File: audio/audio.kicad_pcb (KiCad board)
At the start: 2 copper layers, 67 parts, among them P1 CONN_02X01, P2 CONN_01X04, P3 CONN_02X01, P4 CONN_02X01, U1 PCM2912A, U2 USBAM, U3 MIC, U4 FB, U5 FB, U6 NAU8223, U7 FB, U8 FB, X1 6MHz

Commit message: audio pcb updates
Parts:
- removed U8: FB, SMD_Packages:SMD-1210
- added 1PIN: P***, Connect:1pin, F.Cu at (127.8, 114.1)
- added 2PIN: P***, Connect:1pin, F.Cu at (127.8, 94.1)
- added 3PIN: P***, Connect:1pin, F.Cu at (173.8, 94.1)
- added 4PIN: P***, Connect:1pin, F.Cu at (173.8, 114.1)
- added USB1: AB2_USB, AB2USB:AB2_USB_MICRO_SMD, F.Cu at (124.8, 104.1)
- C1, C10, C11, C12, C13, C14, C15, C16, C17, C3, C4, C5, C8, C9: footprint SMD_Packages:SMD-0603_c -> SMD_Packages:SMD-0603; moved to B.Cu
- C18: value C -> 0.1uF; footprint SMD_Packages:SMD-0603_c -> SMD_Packages:SMD-0603
- C19, C24, C27, C33: value C -> 10uF; footprint SMD_Packages:SMD-0603_c -> SMD_Packages:SMD-0603; moved to B.Cu
- C20, C22, C29, C31: value C -> 1nF; footprint SMD_Packages:SMD-0603_c -> SMD_Packages:SMD-0603; moved to B.Cu
- C21, C23, C28, C30: value C -> 0.47uF; footprint SMD_Packages:SMD-0603_c -> SMD_Packages:SMD-0603; moved to B.Cu
- C25, C26, C32: value C -> 0.1uF; footprint SMD_Packages:SMD-0603_c -> SMD_Packages:SMD-0603; moved to B.Cu
- C6: footprint SMD_Packages:SMD-0603_c -> SMD_Packages:SMD-0603
- JP1: value JUMPER -> HGAIN
- JP2: value JUMPER -> LGAIN
- JP3: value JUMPER -> XMIC
- JP4: value JUMPER -> GS5
- JP5: value JUMPER -> GS0
- L1: moved to B.Cu
- R1, R10, R11, R2, R3, R4, R6, R8: footprint SMD_Packages:SMD-0603_r -> SMD_Packages:SMD-0603; moved to B.Cu
- R5, R7, R9: footprint SMD_Packages:SMD-0603_r -> SMD_Packages:SMD-0603
- SP1: value SPEAKER -> RIGHT
- SP2: value SPEAKER -> LEFT
- U2: value USBAM -> MIC; footprint Connect:USB_A -> MIC:MIC
- U3: value MIC -> FB; footprint MIC:MIC -> MIC:FB-28F0121
- U4, U7: footprint SMD_Packages:SMD-1210 -> MIC:FB-28F0121
- U5: value FB -> NAU8223; footprint SMD_Packages:SMD-1210 -> MIC:QFN20
- U6: value NAU8223 -> FB; footprint MIC:QFN20 -> MIC:FB-28F0121
- X1: footprint SMD_Packages:SMD-1210 -> MIC:FOX6MHZ; moved to B.Cu
- moved D2 70.2 mm to (131.8, 98.6)
- moved C18 68.0 mm to (133.1, 106.9), turned to 180 degrees
- moved C15 62.6 mm to (145.6, 97.1)
- moved JP5 60.3 mm to (156.8, 93.4), turned to 270 degrees
- moved X1 55.5 mm to (137.1, 94.4), turned to 180 degrees
- moved C17 54.9 mm to (149.6, 110.1)
- moved C20 51.7 mm to (162.3, 110.1)
- moved C12 51.6 mm to (145.6, 94.1)
- moved C16 51.6 mm to (158.1, 112.9), turned to 180 degrees
- moved JP1 49.3 mm to (147.1, 93.4), turned to 270 degrees
- moved C10 49.0 mm to (157.8, 94.1)
- moved C14 48.8 mm to (149.6, 99.6)
- moved U2 48.7 mm to (165.3, 93.6), turned to 270 degrees
- moved JP2 48.3 mm to (150.3, 93.4), turned to 270 degrees
- moved JP4 47.3 mm to (153.6, 93.4), turned to 270 degrees
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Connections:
- U2 pad 1: Net-(D1-Pad1) -> XOUT
- U2 pad 2: Net-(R5-Pad2) -> XGAIN
- U2 pad 3: Net-(R6-Pad2) -> Net-(C10-Pad2)
- U2 pad 5: XGND -> Net-(U2-Pad5)
- U2 pad 6: XGND -> Net-(JP3-Pad1)
- U3 pad 1: XOUT -> Net-(C20-Pad1)
- U3 pad 2: XGAIN -> Net-(U3-Pad2)
- U4 pad 1: Net-(C20-Pad1) -> Net-(C22-Pad1)
- U5 pad 1: Net-(C22-Pad1) -> Net-(U3-Pad2)
- U5 pad 2: Net-(U5-Pad2) -> +5VA
- U6 pad 1: Net-(U4-Pad2) -> Net-(C29-Pad1)
- U6 pad 2: +5VA -> Net-(U5-Pad17)
- U7 pad 1: Net-(C29-Pad1) -> Net-(C31-Pad1)
- U7 pad 2: Net-(U6-Pad17) -> Net-(U5-Pad15)
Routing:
- net +5VA: track 0.00 -> 146.8 mm, vias 0 -> 4
- net XGAIN: track 0.00 -> 77.4 mm, vias 0 -> 1
- net Net-(C9-Pad1): track 0.00 -> 69.6 mm, vias 0 -> 1
- net XOUT: track 0.00 -> 67.5 mm, vias 0 -> 1
- net Net-(C16-Pad1): track 0.00 -> 57.4 mm, vias 0 -> 1
- net Net-(R6-Pad2): track 0.00 -> 45.0 mm, vias 0 -> 2
- net EN: track 0.00 -> 43.3 mm, vias 0 -> 1
- net Net-(C2-Pad2): track 0.00 -> 38.7 mm, vias 0 -> 1
- net Net-(P1-Pad1): track 0.00 -> 37.8 mm
- net R_IN: track 0.00 -> 36.8 mm, vias 0 -> 2
- net Net-(C6-Pad2): track 0.00 -> 30.9 mm, vias 0 -> 1
- net Net-(D1-Pad1): track 0.00 -> 30.6 mm, vias 0 -> 1
- net Net-(C20-Pad1): track 0.00 -> 30.4 mm, vias 0 -> 1
- net Net-(C31-Pad1): track 0.00 -> 28.4 mm
- net L_IN: track 0.00 -> 27.1 mm, vias 0 -> 1
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- added copper zone on B.Cu, net XGND
- added copper zone on F.Cu, net XGND
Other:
- board outline added: 52 x 26 mm
- net class normal added: clearance 0.1524, trace_width 0.18, via_dia 0.604, via_drill 0.35
- net class power added: clearance 0.1524, trace_width 0.3, via_dia 0.889, via_drill 0.635
- rule trace_min: 0.254 -> 0.1524
- rule via_min_drill: 0.508 -> 0.35
- rule via_min_size: 0.889 -> 0.604

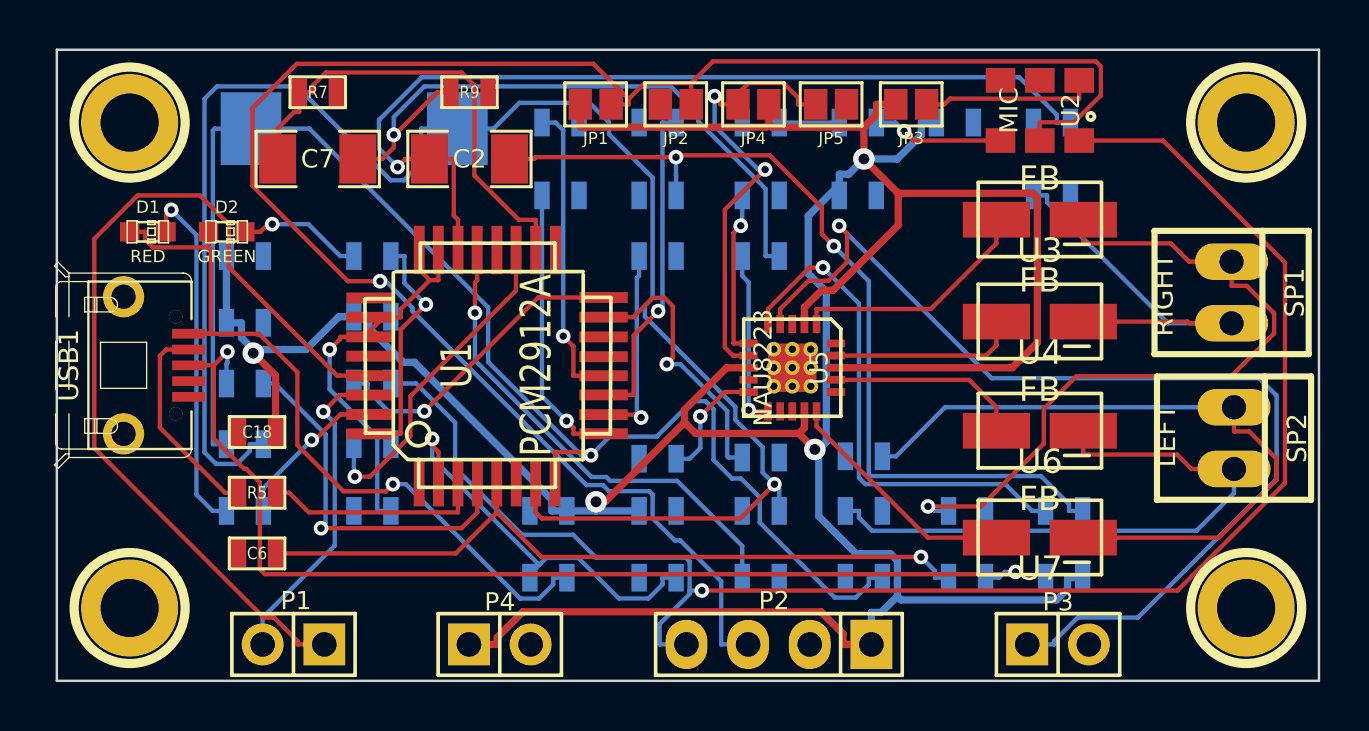
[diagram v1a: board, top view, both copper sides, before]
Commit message: finishing audio pcb layout
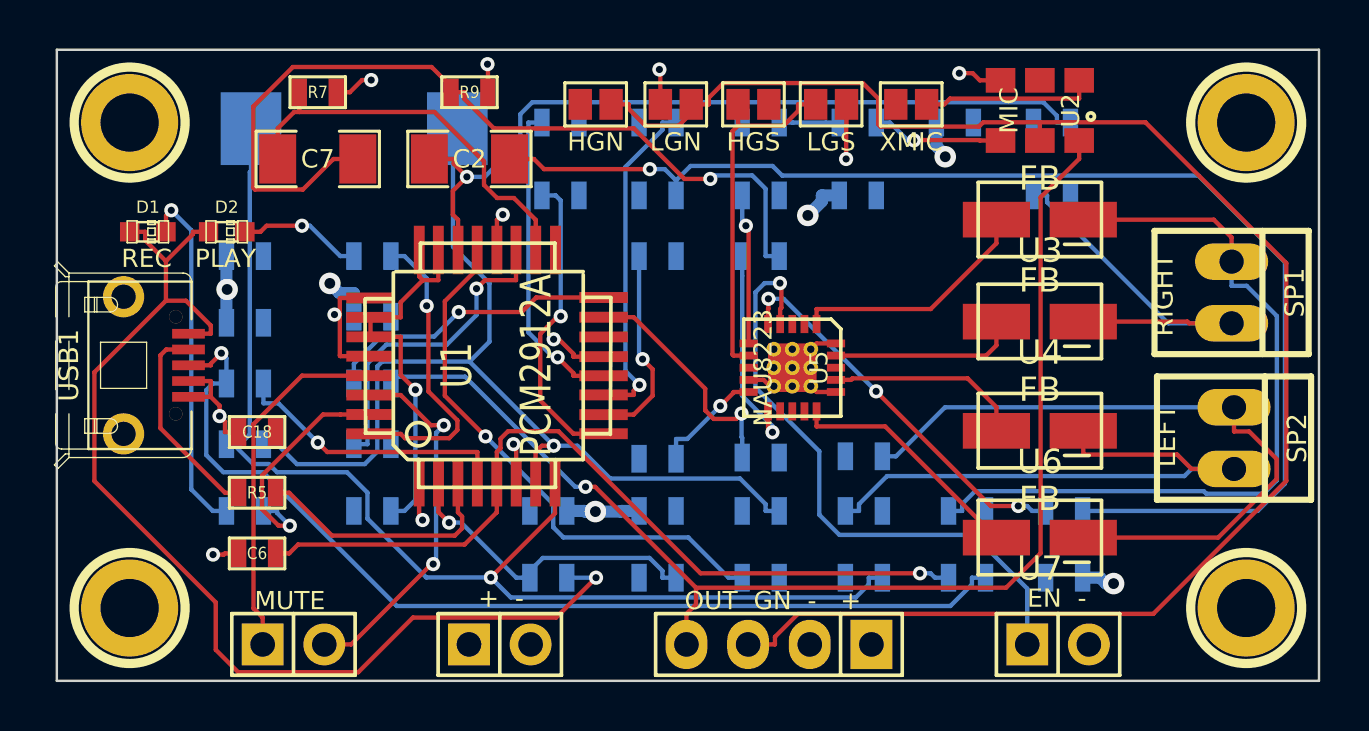
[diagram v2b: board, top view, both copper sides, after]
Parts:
- turned P1 to 270 degrees
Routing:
- net +5VA: track 146.8 -> 12.6 mm, vias 4 -> 6
- net XGND: track 0.00 -> 29.9 mm, vias 0 -> 12
- net Net-(C9-Pad1): track 69.6 -> 40.8 mm
- net Net-(P1-Pad1): track 37.8 -> 14.9 mm
- net EN: track 43.3 -> 25.3 mm
- net XOUT: track 67.5 -> 51.2 mm
- net R_IN: track 36.8 -> 52.7 mm, vias 2 -> 1
- net Net-(D1-Pad1): track 30.6 -> 46.2 mm
- net XGAIN: track 77.4 -> 68.2 mm, vias 1 -> 0
- net L_IN: track 27.1 -> 35.9 mm
- net Net-(C16-Pad1): track 57.4 -> 49.3 mm
- net Net-(C2-Pad2): track 38.7 -> 32.6 mm
- net Net-(C21-Pad1): track 21.1 -> 16.1 mm, vias 1 -> 3
- net Net-(JP4-Pad2): track 18.7 -> 14.8 mm, vias 2 -> 0
- net Net-(R6-Pad1): track 15.4 -> 11.7 mm
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- added copper zone on F.Cu, net +5VA
- removed copper zone on F.Cu, net XGND
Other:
- net class Default: clearance 0.254 -> 0.1524
- net class normal: via_dia 0.604 -> 0.5842; via_drill 0.35 -> 0.3302
- net class power: trace_width 0.3 -> 0.5
- rule trace_clearance: 0.254 -> 0.1524
- rule via_min_drill: 0.35 -> 0.3302
- rule via_min_size: 0.604 -> 0.5842
- board text added: "+ -"
- board text added: "EN -"
- board text added: "HGN"
- board text added: "HGS"
- board text added: "LGN"
- board text added: "LGS"
- board text added: "MUTE"
- board text added: "OUT GN - +"
- board text added: "PLAY"
- board text added: "REC"
- board text added: "XMIC"

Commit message: added logo mod, updated audio pcb, and finished micboard
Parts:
- added G***: LOGO, MIC:LOGO, B.Cu at (150.8, 104.1)

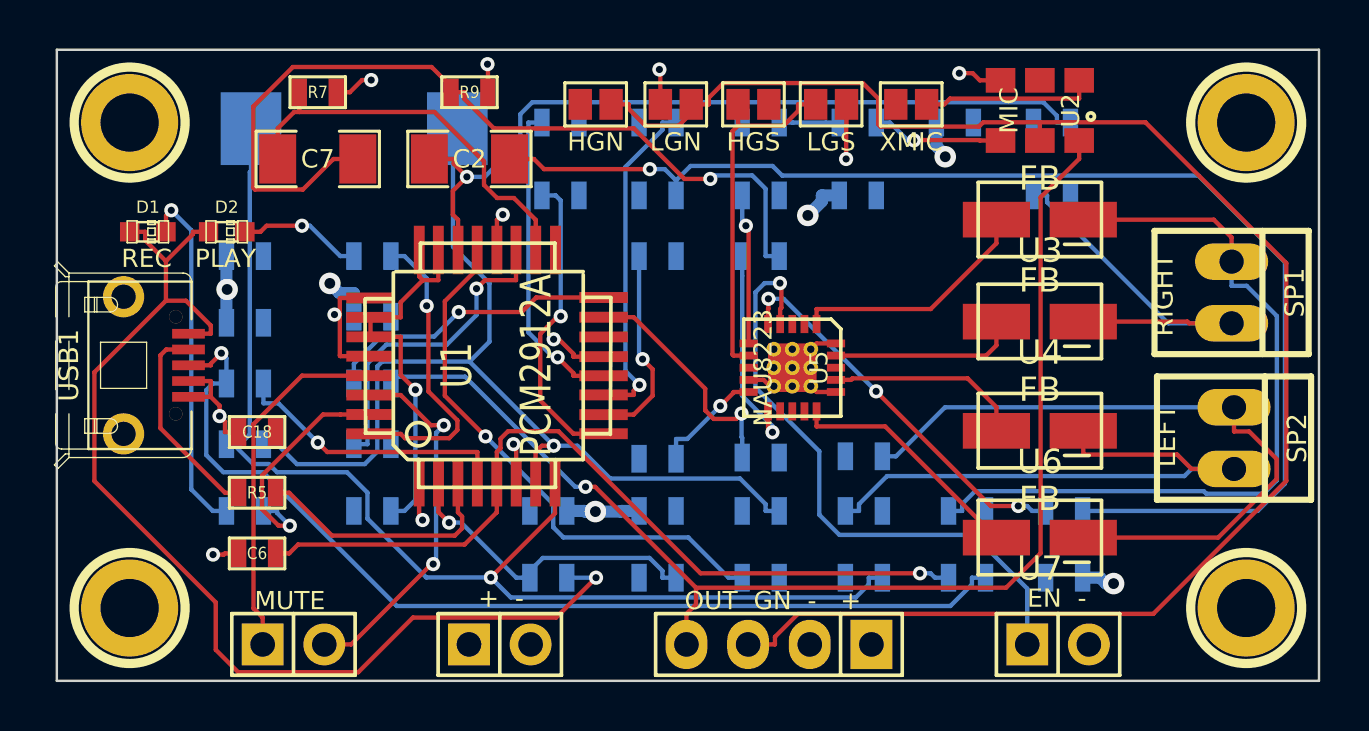
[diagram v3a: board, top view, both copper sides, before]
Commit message: updating audio board to change vias
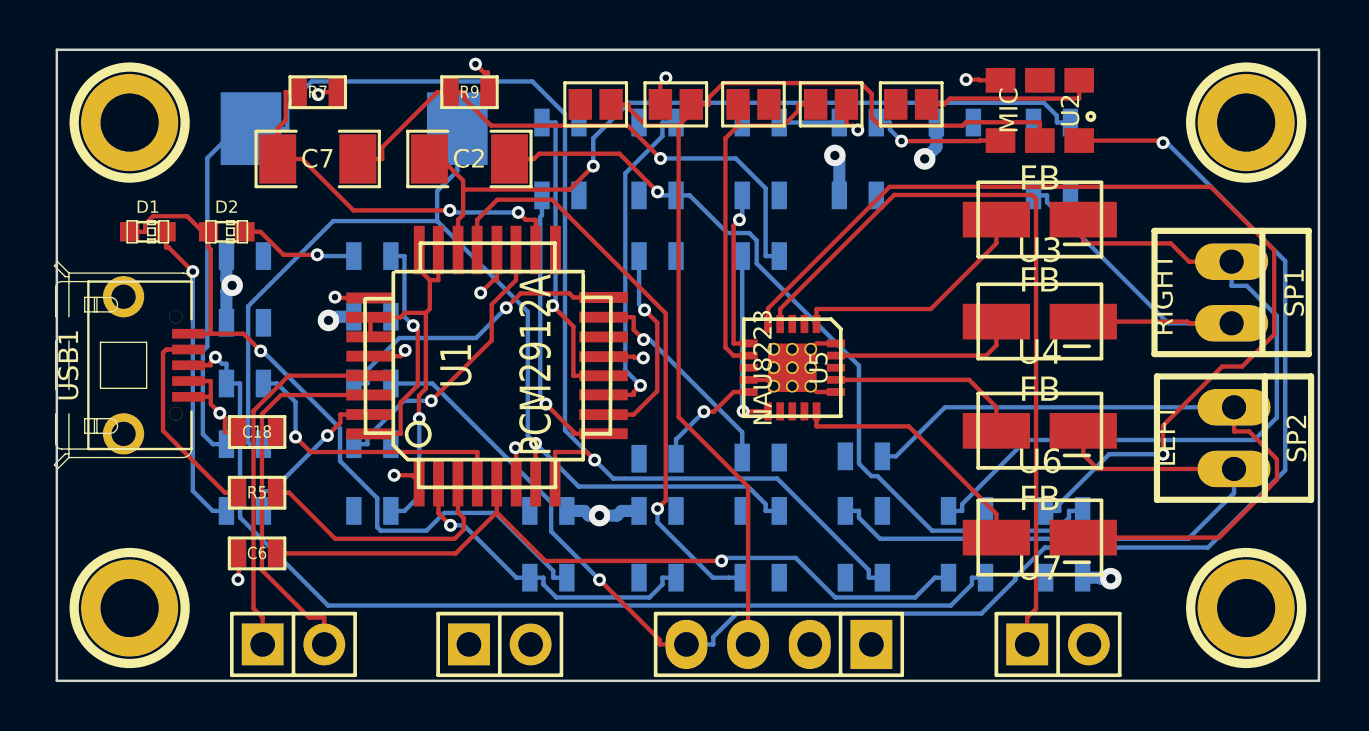
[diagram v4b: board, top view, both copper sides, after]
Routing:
- net Net-(C21-Pad1): track 16.1 -> 41.4 mm, vias 3 -> 1
- net XGAIN: track 68.2 -> 44.0 mm
- net R_IN: track 52.7 -> 33.6 mm
- net Net-(D1-Pad1): track 46.2 -> 30.3 mm
- net XOUT: track 51.2 -> 64.5 mm, vias 1 -> 2
- net L_IN: track 35.9 -> 23.4 mm
- net Net-(C16-Pad1): track 49.3 -> 61.6 mm
- net EN: track 25.3 -> 31.7 mm, vias 1 -> 0
- net XGND: track 29.9 -> 24.9 mm, vias 12 -> 13
- net Net-(R1-Pad1): track 9.71 -> 6.73 mm
- net Net-(R2-Pad1): track 12.4 -> 9.65 mm
- net Net-(C9-Pad1): track 40.8 -> 43.5 mm
- net Net-(C6-Pad2): track 34.0 -> 31.6 mm
- net Net-(C4-Pad2): track 22.5 -> 24.5 mm
- net Net-(D1-Pad2): track 14.6 -> 12.9 mm
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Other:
- net class Default: trace_width 0.254 -> 0.1524; via_dia 0.889 -> 0.5334; via_drill 0.635 -> 0.381
- net class normal: via_dia 0.5842 -> 0.5334; via_drill 0.3302 -> 0.381
- rule via_min_drill: 0.3302 -> 0.381
- rule via_min_size: 0.5842 -> 0.5334
- board text removed: "+ -"
- board text removed: "EN -"
- board text removed: "HGN"
- board text removed: "HGS"
- board text removed: "LGN"
- board text removed: "LGS"
- board text removed: "MUTE"
- board text removed: "OUT GN - +"
- board text removed: "PLAY"
- board text removed: "REC"
- board text removed: "XMIC"

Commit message: correcting audio board vias
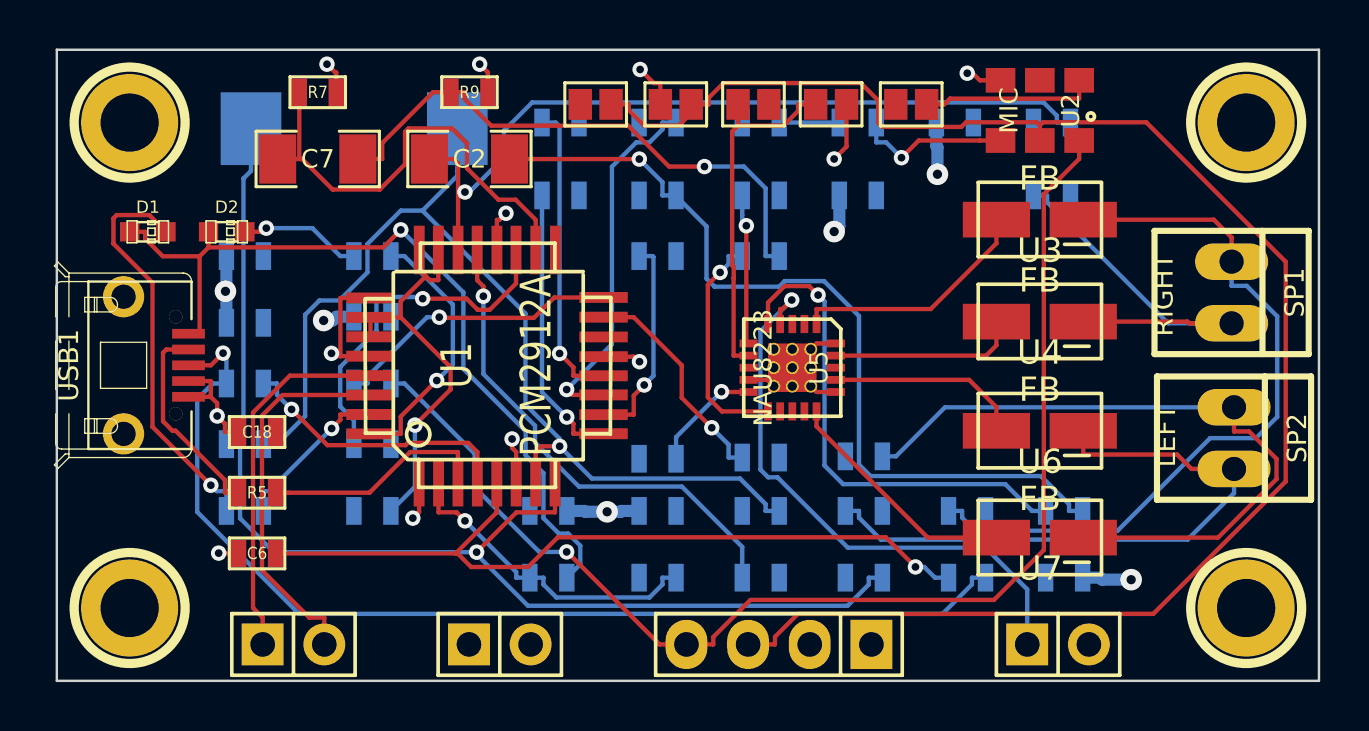
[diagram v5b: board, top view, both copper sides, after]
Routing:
- net XGAIN: track 44.0 -> 68.2 mm
- net Net-(C21-Pad1): track 41.4 -> 20.4 mm
- net XOUT: track 64.5 -> 51.4 mm, vias 2 -> 1
- net Net-(C16-Pad1): track 61.6 -> 50.6 mm
- net EN: track 31.7 -> 24.1 mm, vias 0 -> 1
- net XGND: track 24.9 -> 29.6 mm, vias 13 -> 12
- net Net-(D1-Pad1): track 30.3 -> 34.3 mm
- net Net-(C4-Pad2): track 24.5 -> 20.5 mm
- net Net-(D1-Pad2): track 12.9 -> 16.7 mm
- net Net-(C5-Pad2): track 11.8 -> 14.6 mm
- net Net-(C7-Pad2): track 16.4 -> 19.1 mm, vias 2 -> 0
- net Net-(R6-Pad2): track 41.6 -> 44.1 mm
- net Net-(C30-Pad2): track 7.44 -> 9.46 mm
- net R_IN: track 33.6 -> 35.2 mm
- net Net-(R5-Pad1): track 10.8 -> 9.45 mm
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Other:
- net class Default: via_dia 0.5334 -> 0.635
- net class normal: via_dia 0.5334 -> 0.635
- rule via_min_size: 0.5334 -> 0.635

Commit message: finalizing audio board
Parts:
- moved R8 30.3 mm to (132.6, 107.4), turned to 180 degrees
- moved R10 21.8 mm to (153.8, 112.6), turned to 180 degrees
- moved C27 21.4 mm to (149.6, 112.6)
- moved C30 19.2 mm to (137.8, 110.1), turned to 0 degrees
- moved R3 18.2 mm to (162.4, 110.1)
- moved C1 17.5 mm to (149.6, 97.2), turned to 180 degrees
- moved C3 17.0 mm to (132.6, 112.6)
- moved C4 16.1 mm to (137.8, 112.6), turned to 0 degrees
- moved C14 13.8 mm to (145.0, 112.6)
- moved C20 13.0 mm to (161.9, 97.2), turned to 180 degrees
- moved L1 12.8 mm to (132.6, 110.1), turned to 180 degrees
- moved R1 10.4 mm to (132.6, 99.7)
- moved C31 9.54 mm to (166.4, 112.6)
- moved C11 8.83 mm to (145.0, 107.4)
- moved C28 4.23 mm to (153.8, 107.4)
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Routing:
- net XGND: track 29.6 -> 277.3 mm, vias 12 -> 0
- net +5VA: track 12.9 -> 170.3 mm, vias 6 -> 2
- net XOUT: track 51.4 -> 106.5 mm
- net Net-(R6-Pad2): track 44.1 -> 5.19 mm
- net Net-(P1-Pad1): track 15.2 -> 38.2 mm
- net Net-(P1-Pad2): track 15.7 -> 38.5 mm
- net XGAIN: track 68.2 -> 46.4 mm, vias 0 -> 2
- net Net-(C6-Pad2): track 32.8 -> 13.5 mm
- net Net-(D1-Pad1): track 34.3 -> 17.4 mm
- net EN: track 24.1 -> 40.5 mm
- net Net-(C30-Pad2): track 9.46 -> 23.9 mm
- net Net-(D1-Pad2): track 16.7 -> 5.79 mm
- net Net-(C20-Pad1): track 30.9 -> 20.4 mm
- net Net-(C16-Pad1): track 50.6 -> 41.4 mm, vias 1 -> 2
- net Net-(C13-Pad1): track 15.1 -> 23.0 mm
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- added copper zone on F.Cu, net XGND
- removed copper zone on F.Cu, net +5VA
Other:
- board text added: "+ -"
- board text added: "AUDIO"
- board text added: "EN -"
- board text added: "HGN"
- board text added: "HGS"
- board text added: "LEFT"
- board text added: "LGN"
- board text added: "LGS"
- board text added: "MUTE"
- board text added: "OUT GN - +"
- board text added: "PLAY"
- board text added: "REC"
- board text added: "RIGHT"
- board text added: "XMIC"
